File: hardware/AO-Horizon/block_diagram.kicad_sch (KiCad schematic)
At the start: 0 parts

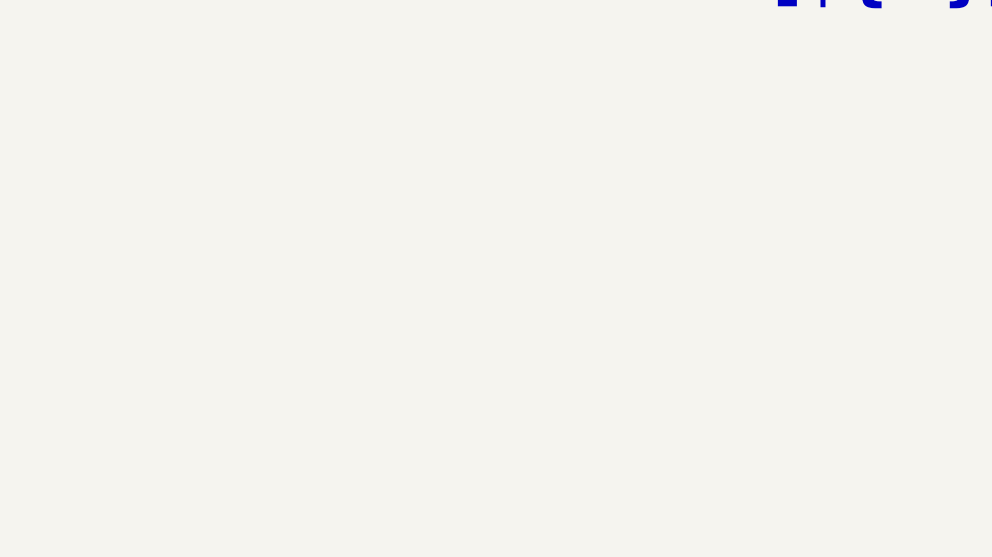
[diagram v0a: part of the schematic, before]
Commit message: feat(power): add TPS62142 3V3 buck and power sheet parts
- power_supplies.kicad_sch: add TPS62142 buck (5V to 3V3) with inductor,
  capacitors and LED, TPS73533DRB LDO (+3.3VA), DF2S6.2CT ESD and a
  6-pin input connector.
- Add the new local libraries to fp-lib-table and sym-lib-table.
- Update AO-Horizon.kicad_sch (embedded font), block_diagram.kicad_sch
  and project settings.

ERC/DRC: NOT_VERIFIED.

Co-Authored-By: Claude Opus 5.5 <noreply@anthropic.com>
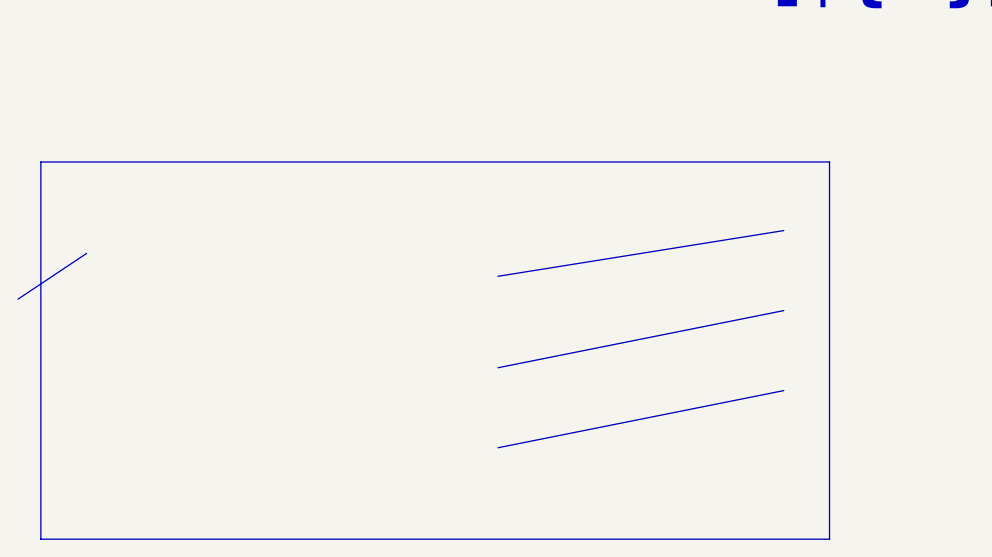
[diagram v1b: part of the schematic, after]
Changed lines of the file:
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@@
 		(comment 1 "Block Diagram")
+	)
+	(rectangle
+		(start 85.09 45.72)
+		(end 172.72 87.63)
+		(stroke
+			(width 0)
+			(type default)
+		)
+		(fill
+			(type none)
+		)
 	)
 	(text "[${#}] ${COMMENT1}"
@@
 		)
 	)
+	(polyline
+		(pts
+			(xy 135.89 68.58) (xy 167.64 62.23)
+		)
+		(stroke
+			(width 0)
+			(type default)
+		)
+	)
+	(polyline
+		(pts
+			(xy 135.89 58.42) (xy 167.64 53.34)
+		)
+		(stroke
+			(width 0)
+			(type default)
+		)
+	)
+	(polyline
+		(pts
+			(xy 135.89 77.47) (xy 167.64 71.12)
+		)
+		(stroke
+			(width 0)
+			(type default)
+		)
+	)
+	(polyline
+		(pts
+			(xy 82.55 60.96) (xy 90.17 55.88)
+		)
+		(stroke
+			(width 0)
+			(type default)
+		)
+	)
 	(image
-		(at 213.36 147.32)
+		(at 212.09 145.415)
 		(scale 0.823638)
 		(data "iVBORw0KGgoAAAANSUhEUgAAEsAAAAyACAIAAADj3OZCAAAQAElEQVR4nOzdCYDOdf4H8G+tITKj"

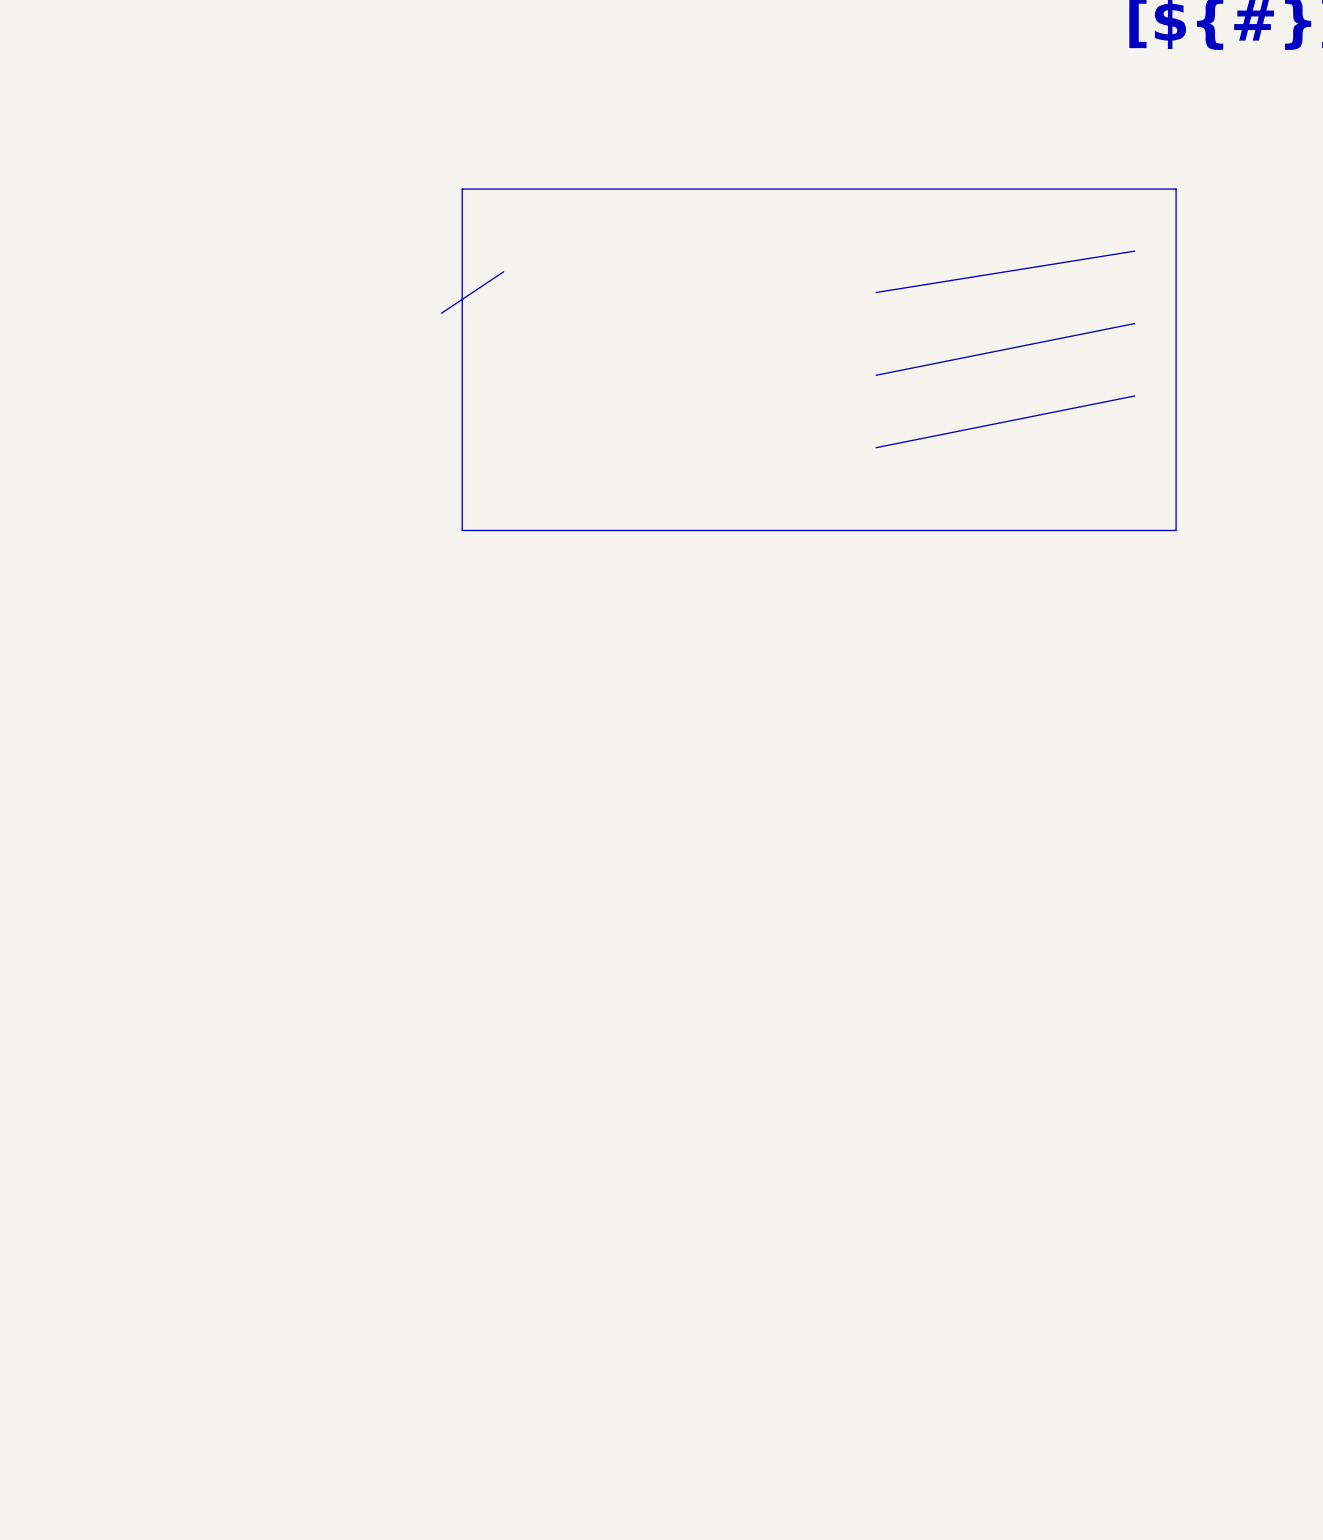
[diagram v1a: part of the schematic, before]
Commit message: feat(sch): update power supply sheet and block diagram
Edits made in KiCad: power_supplies and block_diagram sheets, and a +5V net class for +5V_BUCK.

Co-Authored-By: Claude Opus 5.5 <noreply@anthropic.com>
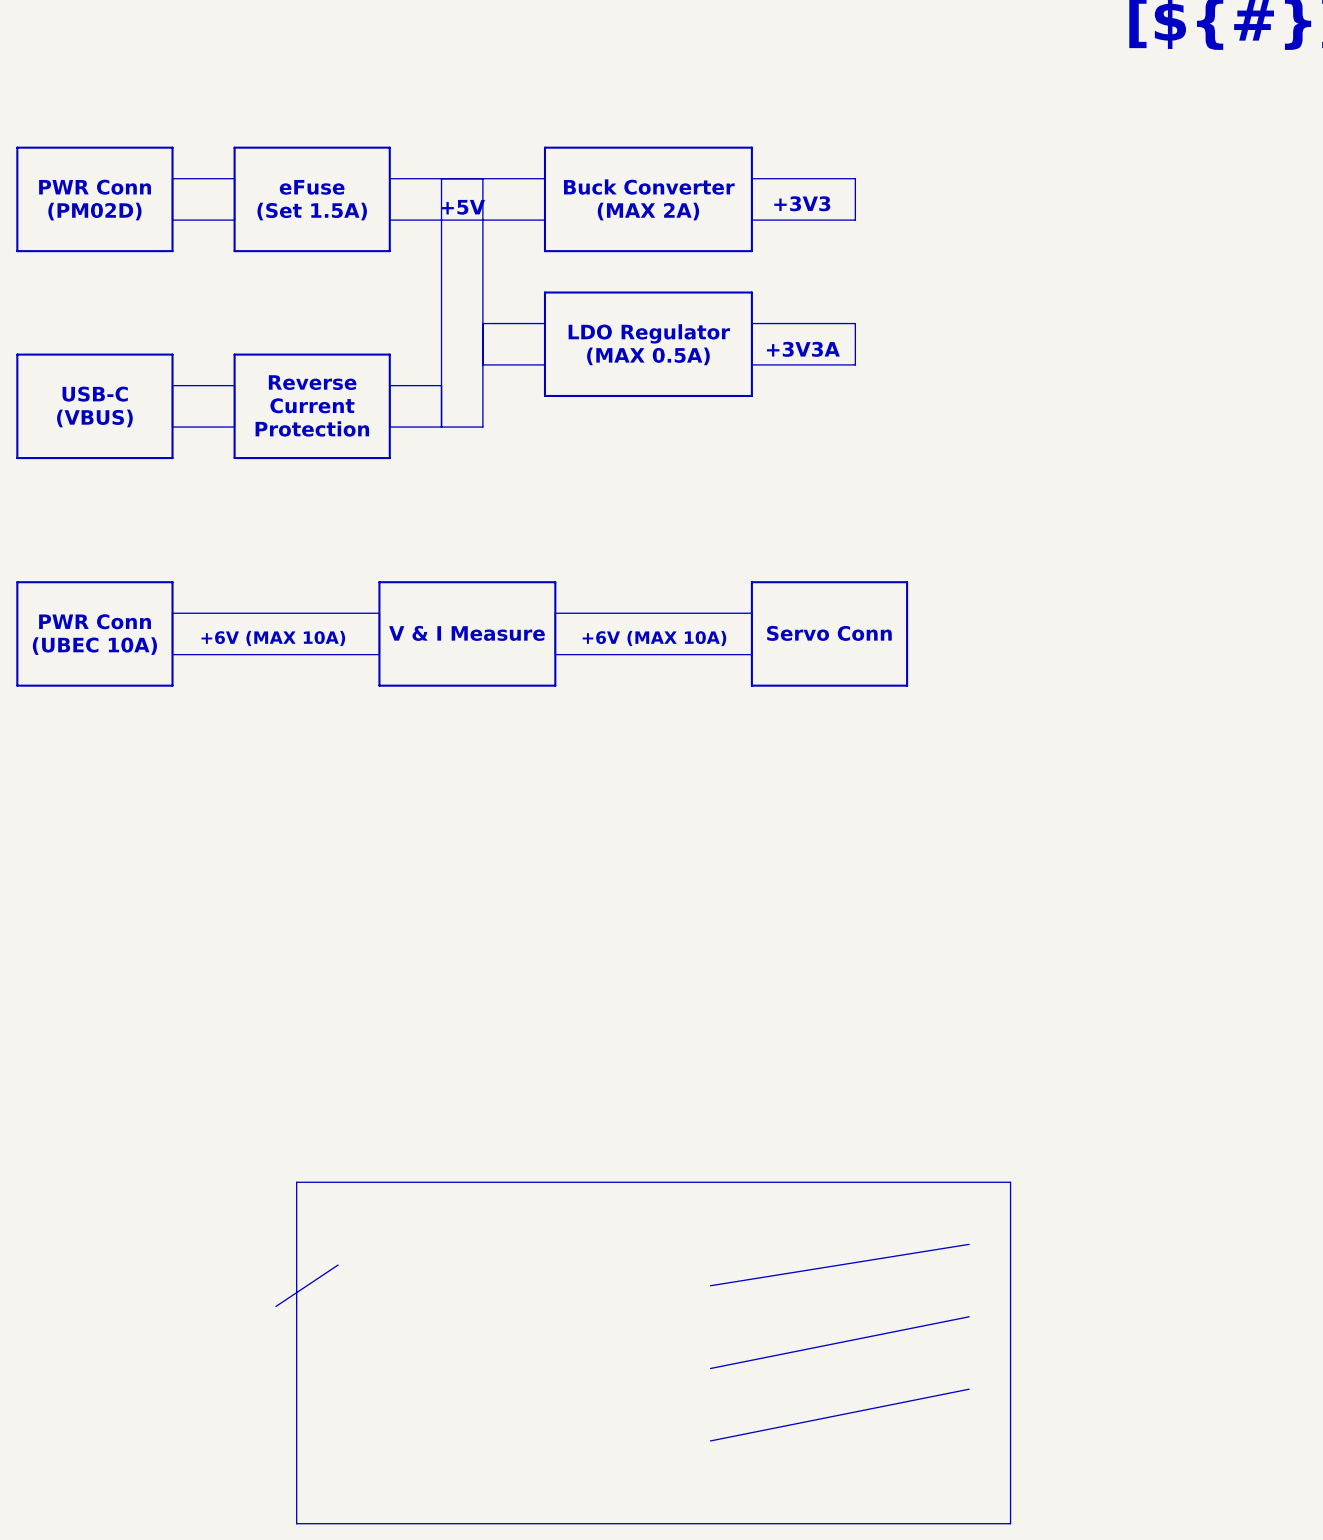
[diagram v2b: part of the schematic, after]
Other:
- note added: "+3V3"
- note added: "+3V3A"
- note added: "+5V"
- note added: "+6V (MAX 10A)"

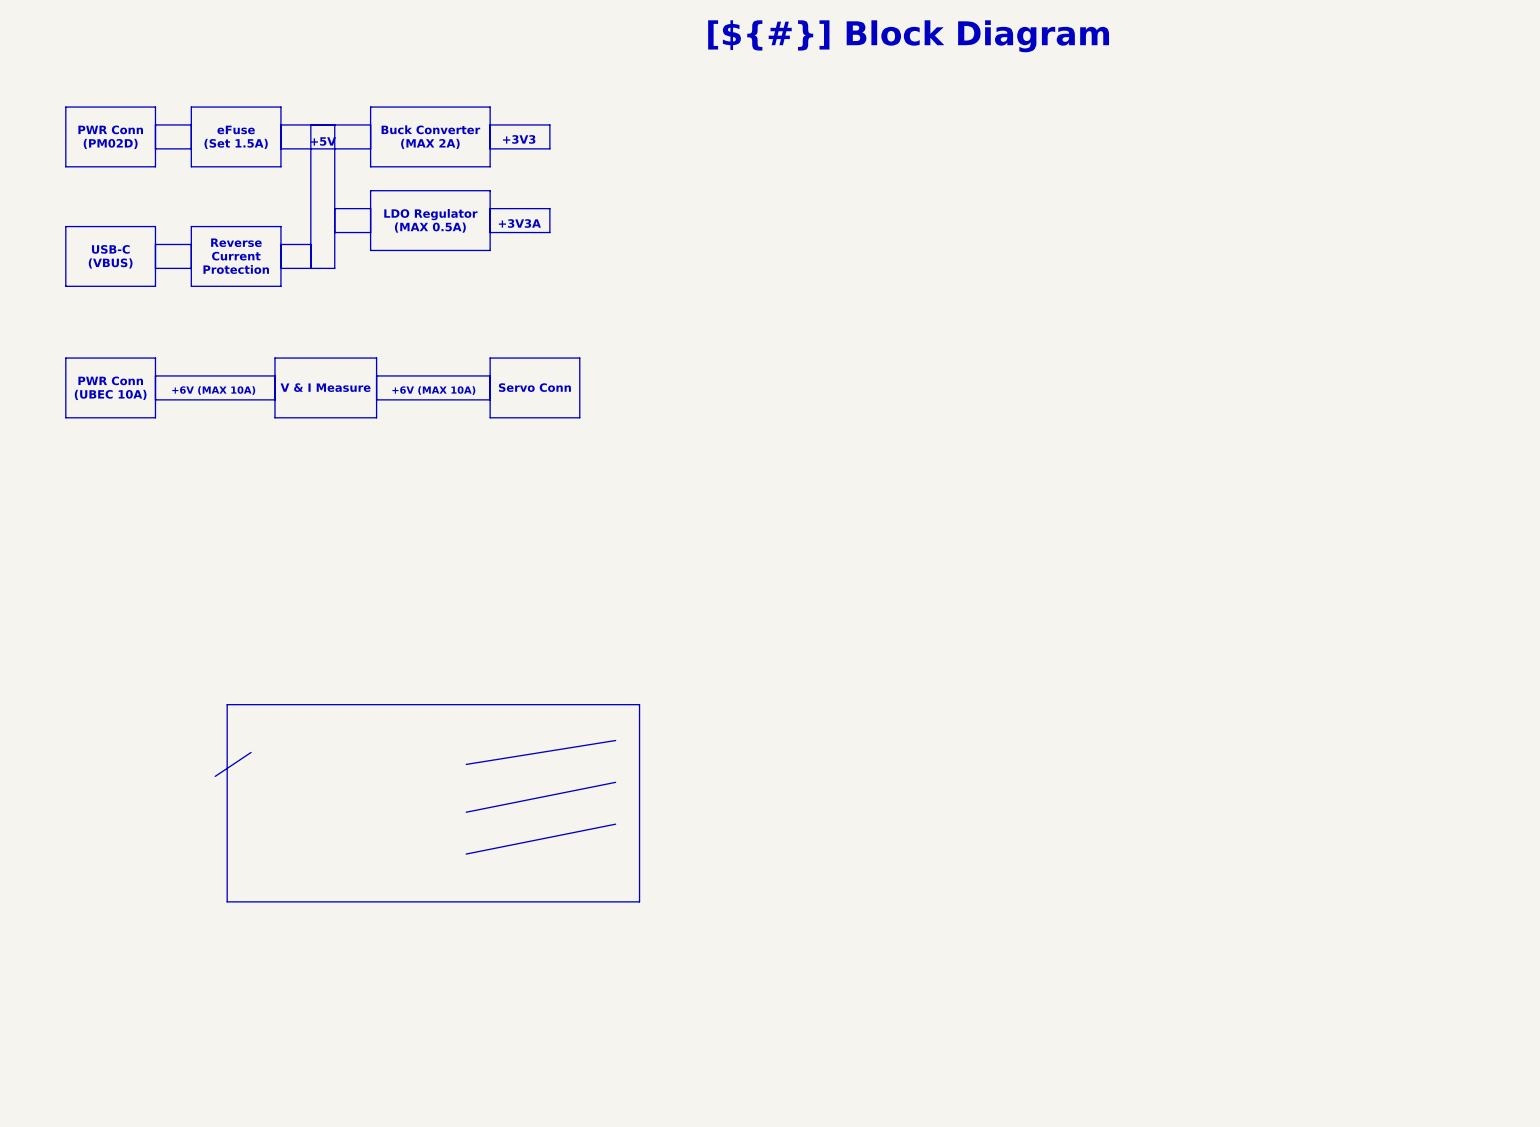
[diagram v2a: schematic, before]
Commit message: feat(sch): label MCU, sensor and connector blocks in block diagram
Co-Authored-By: Claude Opus 5.5 <noreply@anthropic.com>
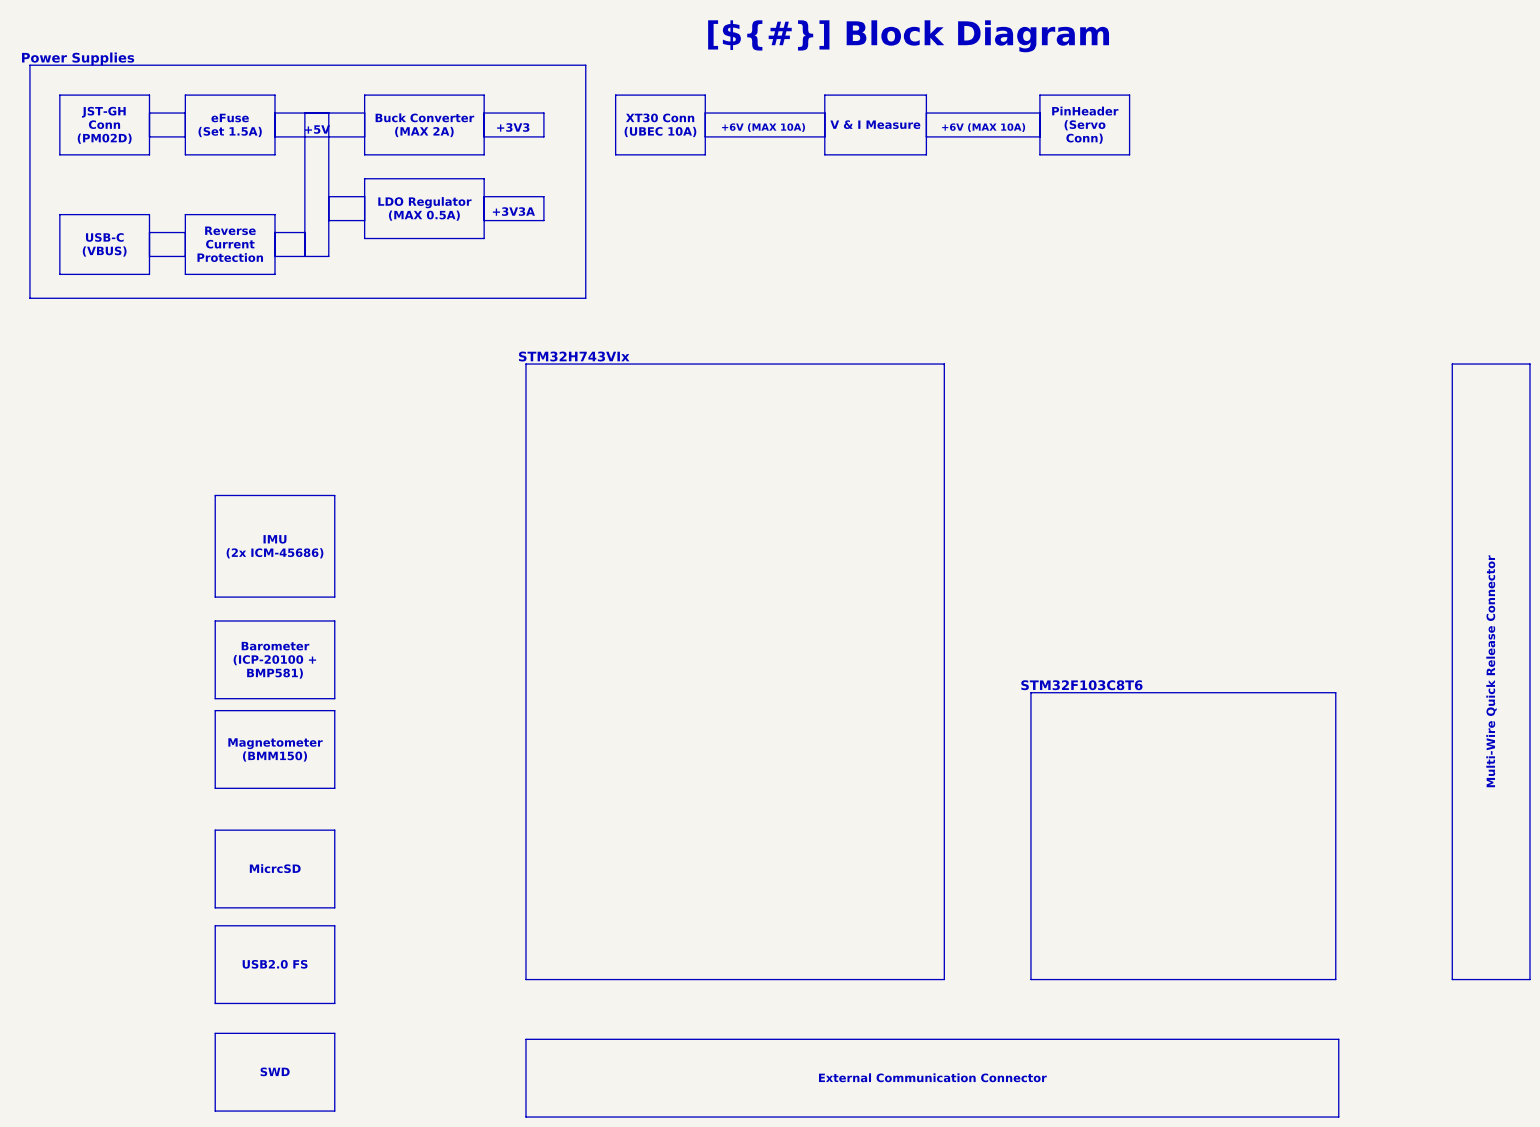
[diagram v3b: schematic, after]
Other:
- note added: "Power Supplies"
- note added: "STM32F103C8T6"
- note added: "STM32H743VIx"
